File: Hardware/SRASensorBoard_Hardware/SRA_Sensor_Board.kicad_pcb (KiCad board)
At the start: 2 copper layers, 124.5 x 92.7 mm, 89 parts, among them J1 USB_A, Q1 BSS138, Q2 BSS138, Q3 BSS138, Q4 BSS138, Q5 BSS138, Q6 BSS138, Q7 Q_PMOS_GDS, Q8 Q_NMOS_GSD, U1 OKI, U2 OKI, U3 FT230XS, U4 TM4C129E_Launchpad

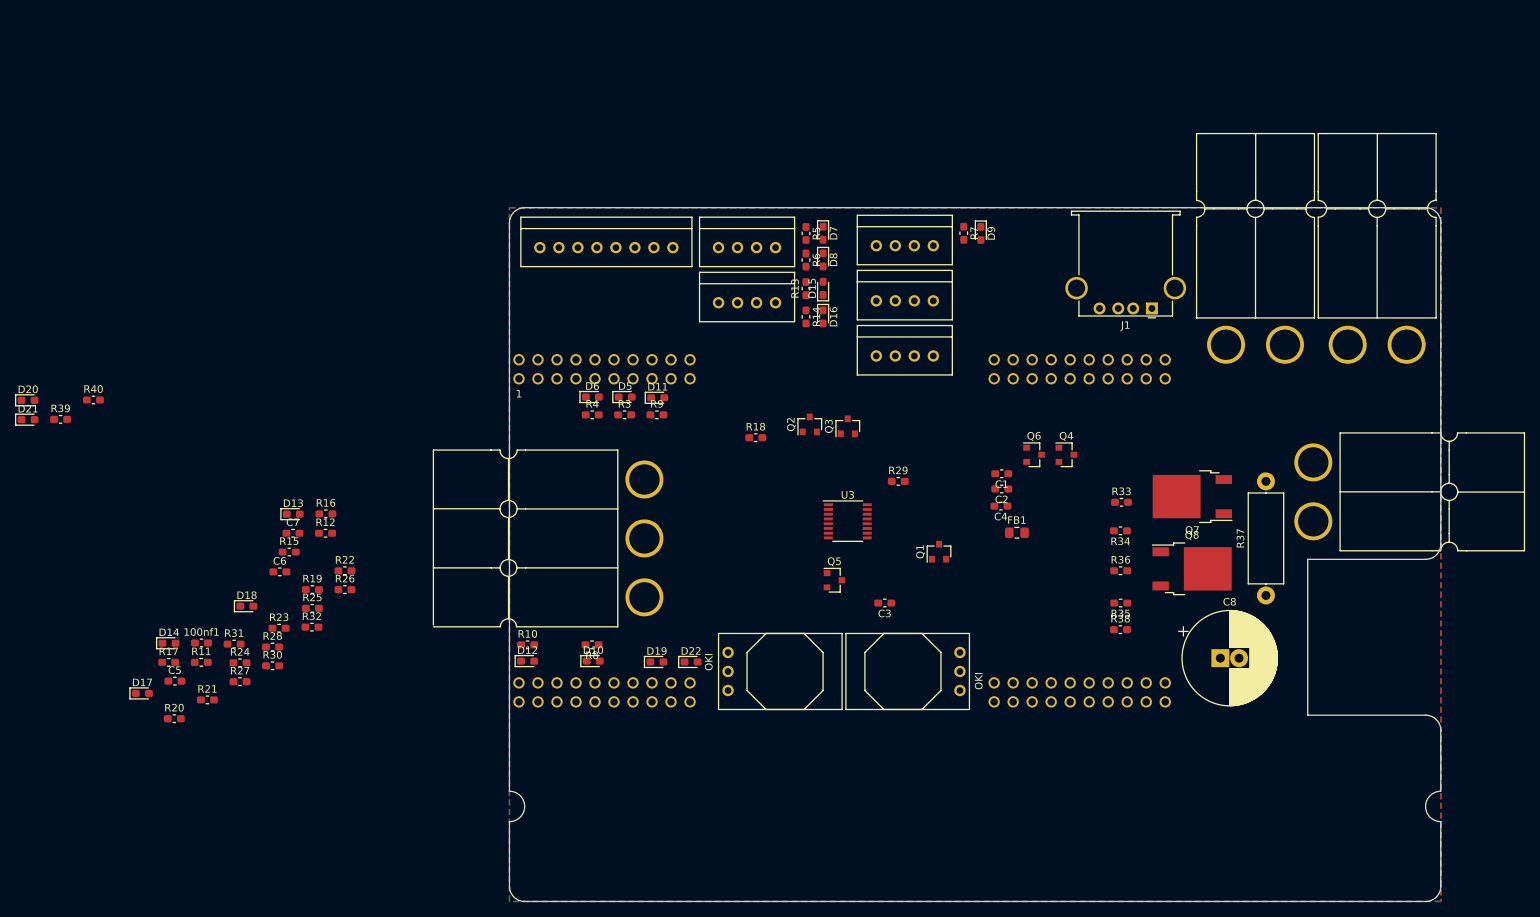
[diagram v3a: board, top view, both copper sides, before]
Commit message: Board Progress 1
Board expanded and mosfets are positioned for wiring
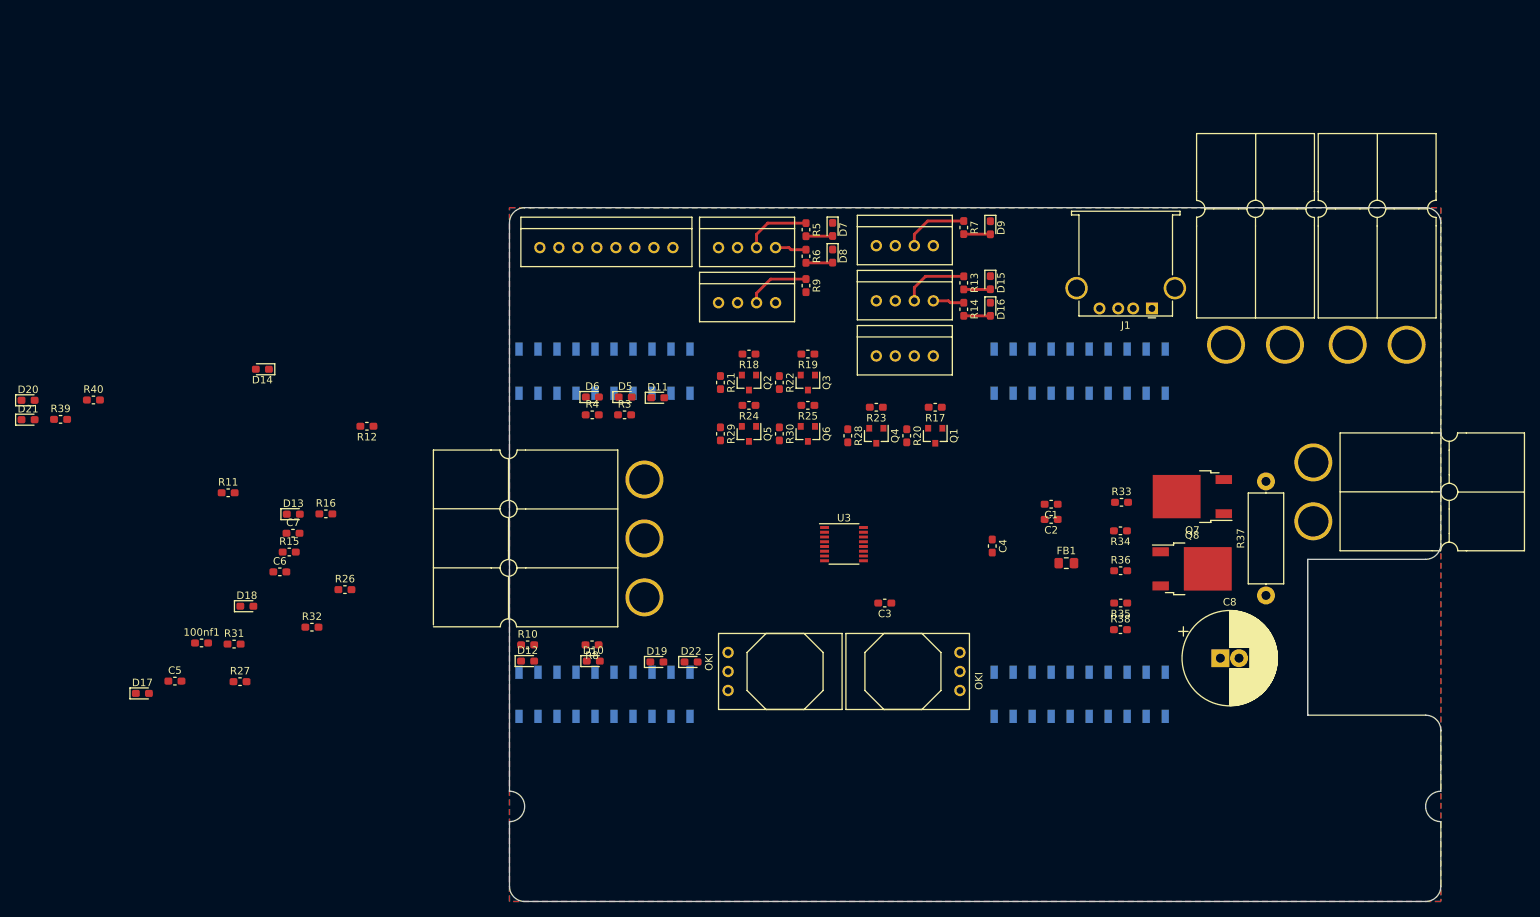
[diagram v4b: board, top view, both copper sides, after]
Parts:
- U4: footprint MRDT_Shields:TM4C129E_Launchpad_FULL_THT_BOTTOM -> MRDT_Shields:TM4C129E_Launchpad_FULL_SMD_BOTTOM
- moved R17 108.0 mm to (148.3, 86.4), turned to 180 degrees
- moved R20 104.9 mm to (144.5, 90.2), turned to 270 degrees
- moved R23 85.1 mm to (140.5, 86.4), turned to 180 degrees
- moved R28 81.9 mm to (136.7, 90.2), turned to 270 degrees
- moved R21 80.6 mm to (119.6, 83.1), turned to 270 degrees
- moved R24 76.2 mm to (123.4, 86.1), turned to 180 degrees
- moved R30 74.5 mm to (127.5, 89.9), turned to 270 degrees
- moved R19 73.3 mm to (131.3, 79.2), turned to 180 degrees
- moved R25 71.6 mm to (131.3, 86.1), turned to 180 degrees
- moved R22 63.3 mm to (127.5, 83.1), turned to 270 degrees
- moved D14 38.7 mm to (58.4, 81.3), turned to 180 degrees
- moved Q6 30.4 mm to (131.3, 89.9), turned to 270 degrees
- moved R9 26.4 mm to (131.1, 70.1), turned to 270 degrees
- moved Q4 25.5 mm to (140.5, 90.2), turned to 270 degrees
- moved R29 24.6 mm to (119.6, 89.9), turned to 270 degrees
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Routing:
- net O2_TX: track 0.00 -> 9.00 mm
- net NO2_TX: track 0.00 -> 9.00 mm
- net NO_SCL: track 0.00 -> 8.86 mm
- net CO2_TX: track 0.00 -> 8.66 mm
- net O2_RX: track 0.00 -> 4.18 mm
- net NO2_RX: track 0.00 -> 4.17 mm
- net Net-(D9-Pad2): track 0.00 -> 3.57 mm
- net Net-(D7-Pad2): track 0.00 -> 3.57 mm
- net Net-(D8-Pad2): track 0.00 -> 3.57 mm
- net Net-(D15-Pad2): track 0.00 -> 3.57 mm
- net Net-(D16-Pad2): track 0.00 -> 3.56 mm

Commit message: Broad Progress 2-oof
Pre-oops need to add 6 mosfets for spectrometer
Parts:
- C8: footprint Capacitor_THT:CP_Radial_D12.5mm_P2.50mm -> Capacitor_THT:CP_Radial_D12.5mm_P5.00mm
- C9: renamed from 100nf1; value C -> 100nf
- Conn1, Conn3: moved to B.Cu
- moved D20 165.0 mm to (187.7, 123.2), turned to 180 degrees
- moved D21 164.8 mm to (187.7, 125.0), turned to 180 degrees
- moved R39 157.0 mm to (184.0, 125.0)
- moved R40 153.8 mm to (184.0, 126.7)
- moved R4 108.3 mm to (210.3, 77.5), turned to 180 degrees
- moved D6 107.9 mm to (210.3, 80.3), turned to 180 degrees
- moved D19 107.0 mm to (213.0, 87.6), turned to 180 degrees
- moved R11 100.5 mm to (152.1, 77.0), turned to 270 degrees
- moved D14 97.3 mm to (155.7, 80.4), turned to 270 degrees
- moved D13 96.1 mm to (155.7, 77.0), turned to 270 degrees
- moved C8 82.8 mm to (109.0, 90.7)
- moved D17 81.6 mm to (124.0, 123.7), turned to 180 degrees
- moved R3 80.2 mm to (186.4, 77.5), turned to 180 degrees
- moved R12 80.2 mm to (152.1, 80.4), turned to 270 degrees
- moved D5 79.7 mm to (186.4, 80.3), turned to 180 degrees
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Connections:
- Q1 pad 2: N2O_TX -> TIVA_N2O_TX
- Q4 pad 2: N2O_RX -> TIVA_N2O_RX
- R17 pad 2: N2O_TX -> TIVA_N2O_TX
- R23 pad 2: N2O_RX -> TIVA_N2O_RX
- U4 pad PP0: N2O_RX -> TIVA_N2O_RX
- U4 pad PP1: N2O_TX -> TIVA_N2O_TX
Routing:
- net +5V: track 0.00 -> 144.1 mm, vias 0 -> 2
- net +3V3: track 0.00 -> 111.2 mm, vias 0 -> 10
- net NO_SDA: track 0.00 -> 100.4 mm
- net +12V: track 0.00 -> 84.9 mm, vias 0 -> 2
- net LED_Enable: track 0.00 -> 79.3 mm, vias 0 -> 3
- net EOS: track 0.00 -> 75.5 mm
- net Start_Pulse: track 0.00 -> 75.3 mm, vias 0 -> 1
- net Trigger_Pulse: track 0.00 -> 72.1 mm, vias 0 -> 3
- net Clock_Pulse: track 0.00 -> 68.1 mm, vias 0 -> 3
- net Video: track 0.00 -> 64.6 mm, vias 0 -> 3
- net +24V: track 0.00 -> 54.8 mm, vias 0 -> 1
- net TIVA_O2_TX: track 0.00 -> 53.8 mm, vias 0 -> 1
- net TIVA_USB_RX: track 0.00 -> 48.5 mm, vias 0 -> 3
- net N2O_TX: track 0.00 -> 47.1 mm, vias 0 -> 2
- net NO2_RX: track 4.17 -> 50.3 mm, vias 0 -> 2
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- added copper zone on F.Cu, net +24V
- added copper zone on F.Cu, net Net-(Q7-Pad1)
- added copper zone on F.Cu, net Net-(Q8-Pad3)

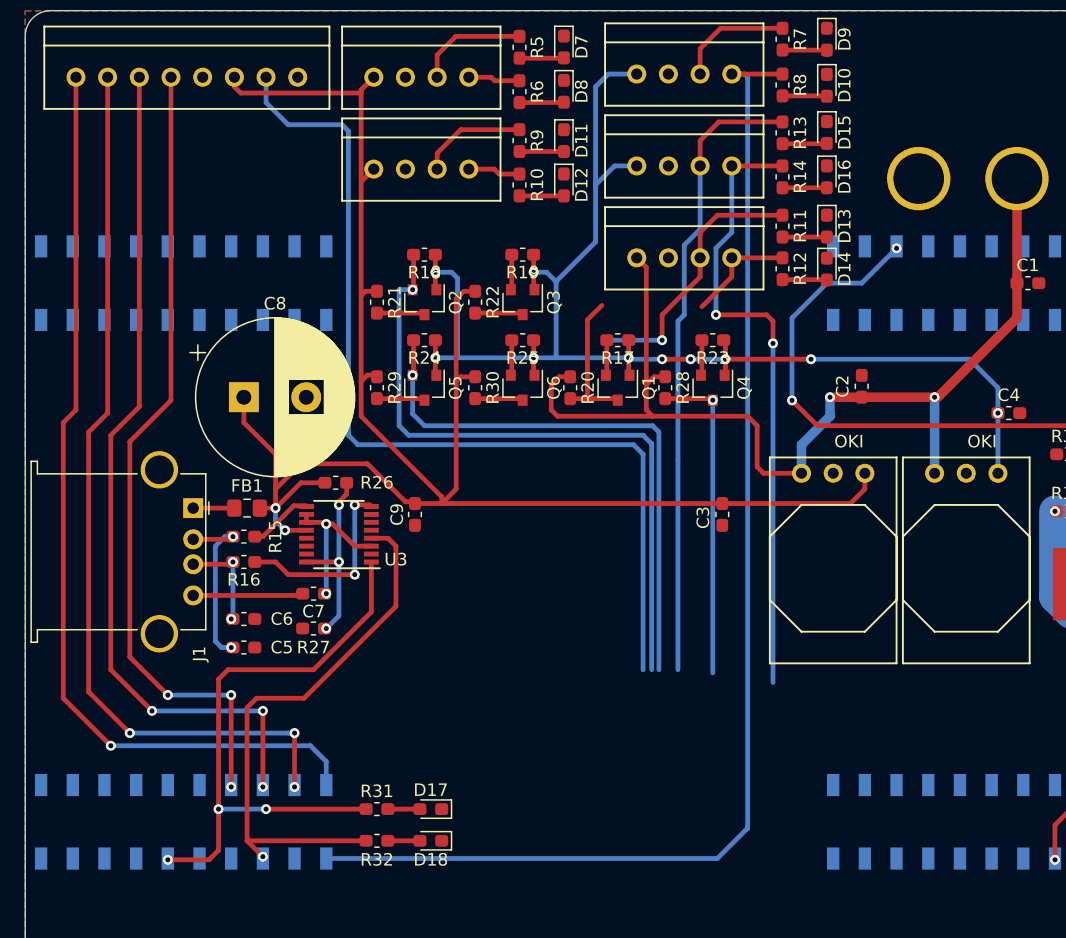
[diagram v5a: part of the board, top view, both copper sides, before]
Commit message: Board Progress 3
New mosfets are in but old mosfets need some clean up
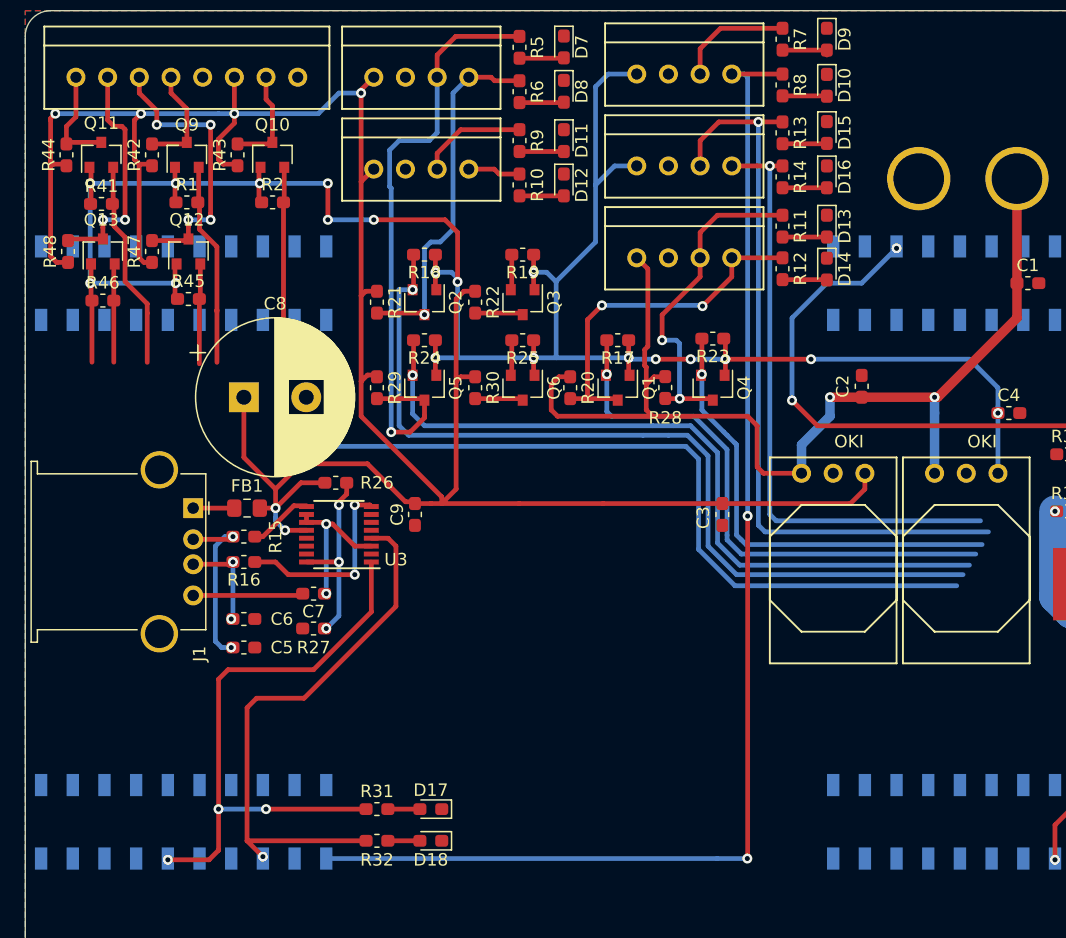
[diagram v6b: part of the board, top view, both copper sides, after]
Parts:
- added Q10: BSS138, Package_TO_SOT_SMD:SOT-23, F.Cu at (111.3, 71.2)
- added Q11: BSS138, Package_TO_SOT_SMD:SOT-23, F.Cu at (97.5, 71.2)
- added Q12: BSS138, Package_TO_SOT_SMD:SOT-23, F.Cu at (104.5, 79.0)
- added Q13: BSS138, Package_TO_SOT_SMD:SOT-23, F.Cu at (97.7, 79.0)
- added Q9: BSS138, Package_TO_SOT_SMD:SOT-23, F.Cu at (104.4, 71.2)
- added R1: 10K, Resistor_SMD:R_0603_1608Metric_Pad1.05x0.95mm_HandSolder, F.Cu at (104.4, 75.1)
- added R2: 10K, Resistor_SMD:R_0603_1608Metric_Pad1.05x0.95mm_HandSolder, F.Cu at (111.3, 75.1)
- added R41: 10K, Resistor_SMD:R_0603_1608Metric_Pad1.05x0.95mm_HandSolder, F.Cu at (97.5, 75.2)
- added R42: 10K, Resistor_SMD:R_0603_1608Metric_Pad1.05x0.95mm_HandSolder, F.Cu at (101.6, 71.2)
- added R43: 10K, Resistor_SMD:R_0603_1608Metric_Pad1.05x0.95mm_HandSolder, F.Cu at (108.5, 71.2)
- added R44: 10K, Resistor_SMD:R_0603_1608Metric_Pad1.05x0.95mm_HandSolder, F.Cu at (94.7, 71.2)
- added R45: 10K, Resistor_SMD:R_0603_1608Metric_Pad1.05x0.95mm_HandSolder, F.Cu at (104.5, 82.8)
- added R46: 10K, Resistor_SMD:R_0603_1608Metric_Pad1.05x0.95mm_HandSolder, F.Cu at (97.7, 82.9)
- added R47: 10K, Resistor_SMD:R_0603_1608Metric_Pad1.05x0.95mm_HandSolder, F.Cu at (101.6, 79.0)
- added R48: 10K, Resistor_SMD:R_0603_1608Metric_Pad1.05x0.95mm_HandSolder, F.Cu at (94.9, 79.0)
- moved R23 0.13 mm to (146.6, 86.0)
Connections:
- U4 pad PA6: Clock_Pulse -> TIVA_Clock_Pulse
- U4 pad PD2: EOS -> TIVA_EOS
- U4 pad PD7: Video -> TIVA_Video
- U4 pad PM4: Trigger_Pulse -> TIVA_Trigger_Pulse
- U4 pad PM5: Start_Pulse -> TIVA_Start_Pulse
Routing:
- net TIVA_EOS: track 0.00 -> 85.3 mm, vias 0 -> 1
- net +3V3: track 111.2 -> 182.0 mm, vias 10 -> 19
- net EOS: track 75.5 -> 8.46 mm
- net Start_Pulse: track 75.3 -> 8.69 mm, vias 1 -> 0
- net Video: track 64.6 -> 8.77 mm, vias 3 -> 0
- net Trigger_Pulse: track 72.1 -> 18.7 mm, vias 3 -> 2
- net +5V: track 144.1 -> 195.7 mm, vias 2 -> 6
- net Clock_Pulse: track 68.1 -> 22.8 mm, vias 3 -> 4
- net TIVA_N2O_TX: track 2.84 -> 44.4 mm, vias 0 -> 1
- net O2_TX: track 12.9 -> 48.9 mm, vias 0 -> 1
- net TIVA_N2O_RX: track 2.84 -> 36.9 mm, vias 0 -> 1
- net O2_RX: track 8.04 -> 29.0 mm, vias 0 -> 1
- net N2O_TX: track 47.1 -> 26.9 mm
- net TIVA_Start_Pulse: track 0.00 -> 16.9 mm
- net TIVA_Video: track 0.00 -> 16.5 mm
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
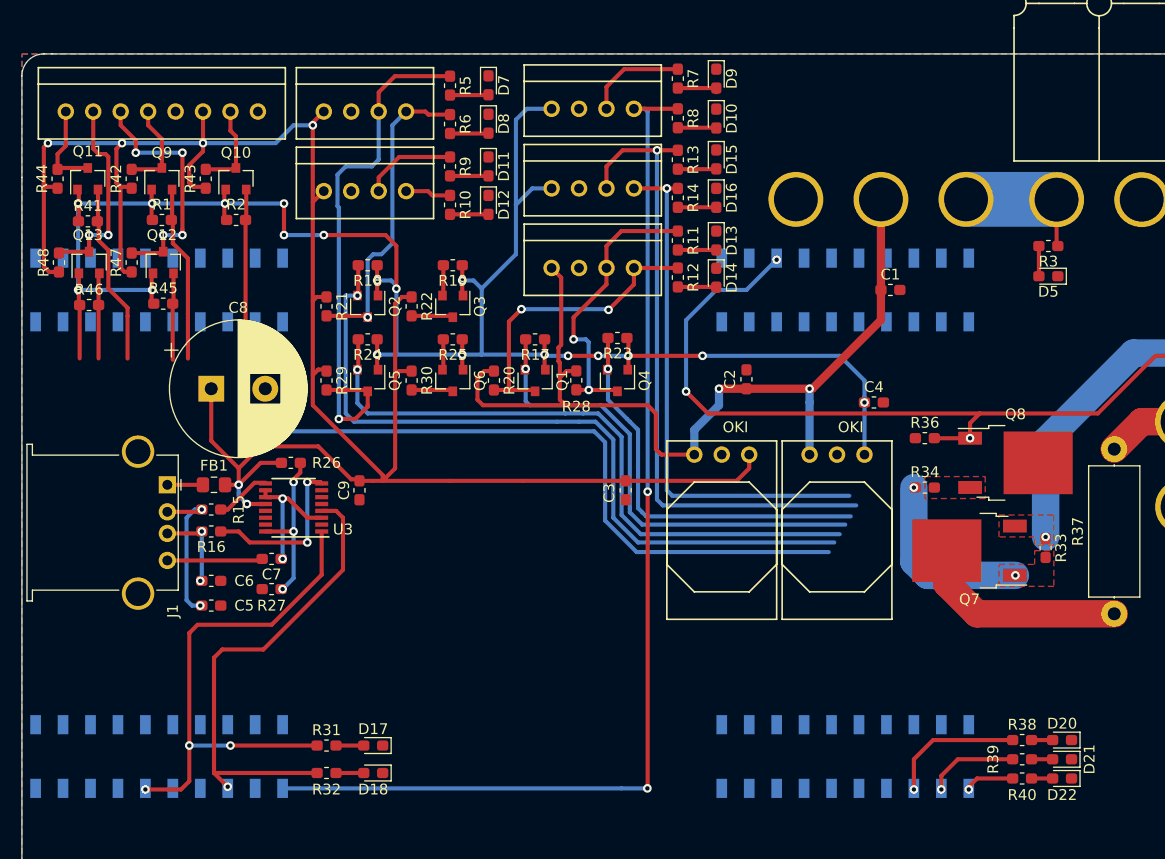
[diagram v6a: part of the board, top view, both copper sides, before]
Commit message: Board Progress 4
Finished mosfets and cleaned up traces
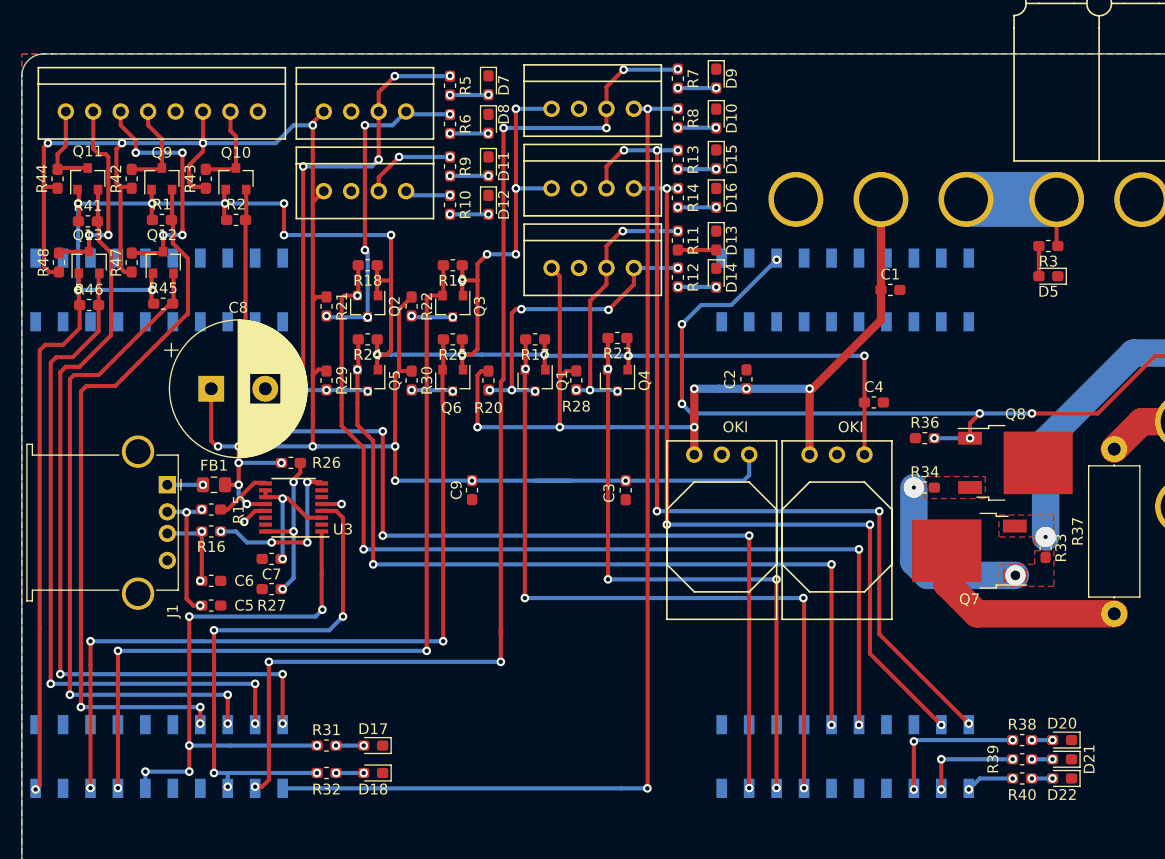
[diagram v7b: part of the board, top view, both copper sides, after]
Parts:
- moved C9 10.4 mm to (133.1, 100.1)
- moved R20 0.51 mm to (134.6, 89.9)
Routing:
- net NO_SCL: track 9.31 -> 104.7 mm, vias 0 -> 7
- net TIVA_CO2_TX: track 2.84 -> 78.6 mm, vias 0 -> 3
- net TIVA_CO2_RX: track 2.84 -> 74.5 mm, vias 0 -> 3
- net TIVA_Start_Pulse: track 16.9 -> 73.3 mm, vias 0 -> 3
- net TIVA_Trigger_Pulse: track 7.91 -> 63.4 mm, vias 0 -> 3
- net TIVA_Clock_Pulse: track 8.03 -> 61.7 mm, vias 0 -> 3
- net TIVA_Video: track 16.5 -> 67.0 mm, vias 0 -> 3
- net +3V3: track 182.0 -> 228.3 mm
- net NO2_RX: track 49.1 -> 75.3 mm, vias 1 -> 5
- net NO2_TX: track 60.2 -> 86.3 mm, vias 1 -> 6
- net TIVA_N2O_TX: track 44.4 -> 67.1 mm, vias 1 -> 4
- net TIVA_O2_TX: track 69.2 -> 90.6 mm, vias 1 -> 4
- net TIVA_N2O_RX: track 36.9 -> 57.2 mm, vias 1 -> 4
- net TIVA_O2_RX: track 59.8 -> 78.7 mm, vias 1 -> 4
- net TIVA_EOS: track 85.3 -> 102.1 mm, vias 1 -> 5
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
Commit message: Board Progress 5 (First revison)
Finished Rev 1
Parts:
- added G***: LOGO, MRDT_Silkscreens:z_sig_Evan_Seabaugh_44mmx13.5mm, F.Cu at (175.8, 147.1)
- added G***: MRDT, MRDT_Silkscreens:0_MRDT_Logo_20mm, F.Cu at (203.3, 138.9)
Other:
- board text added: "I did a thing©"
- board text added: "Science Board Rev 1 Mars Rover, 2021 Missouri S&T Evan Seabaugh & Anthony"
